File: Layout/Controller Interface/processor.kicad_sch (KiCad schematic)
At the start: 27 parts, among them J1 USB_C_Receptacle_USB2.0, SW3 SW_PAIR, SW4 SW_BOOT, U1 W25Q32JVSS, U2 RP2040, Y2 Crystal_GND24

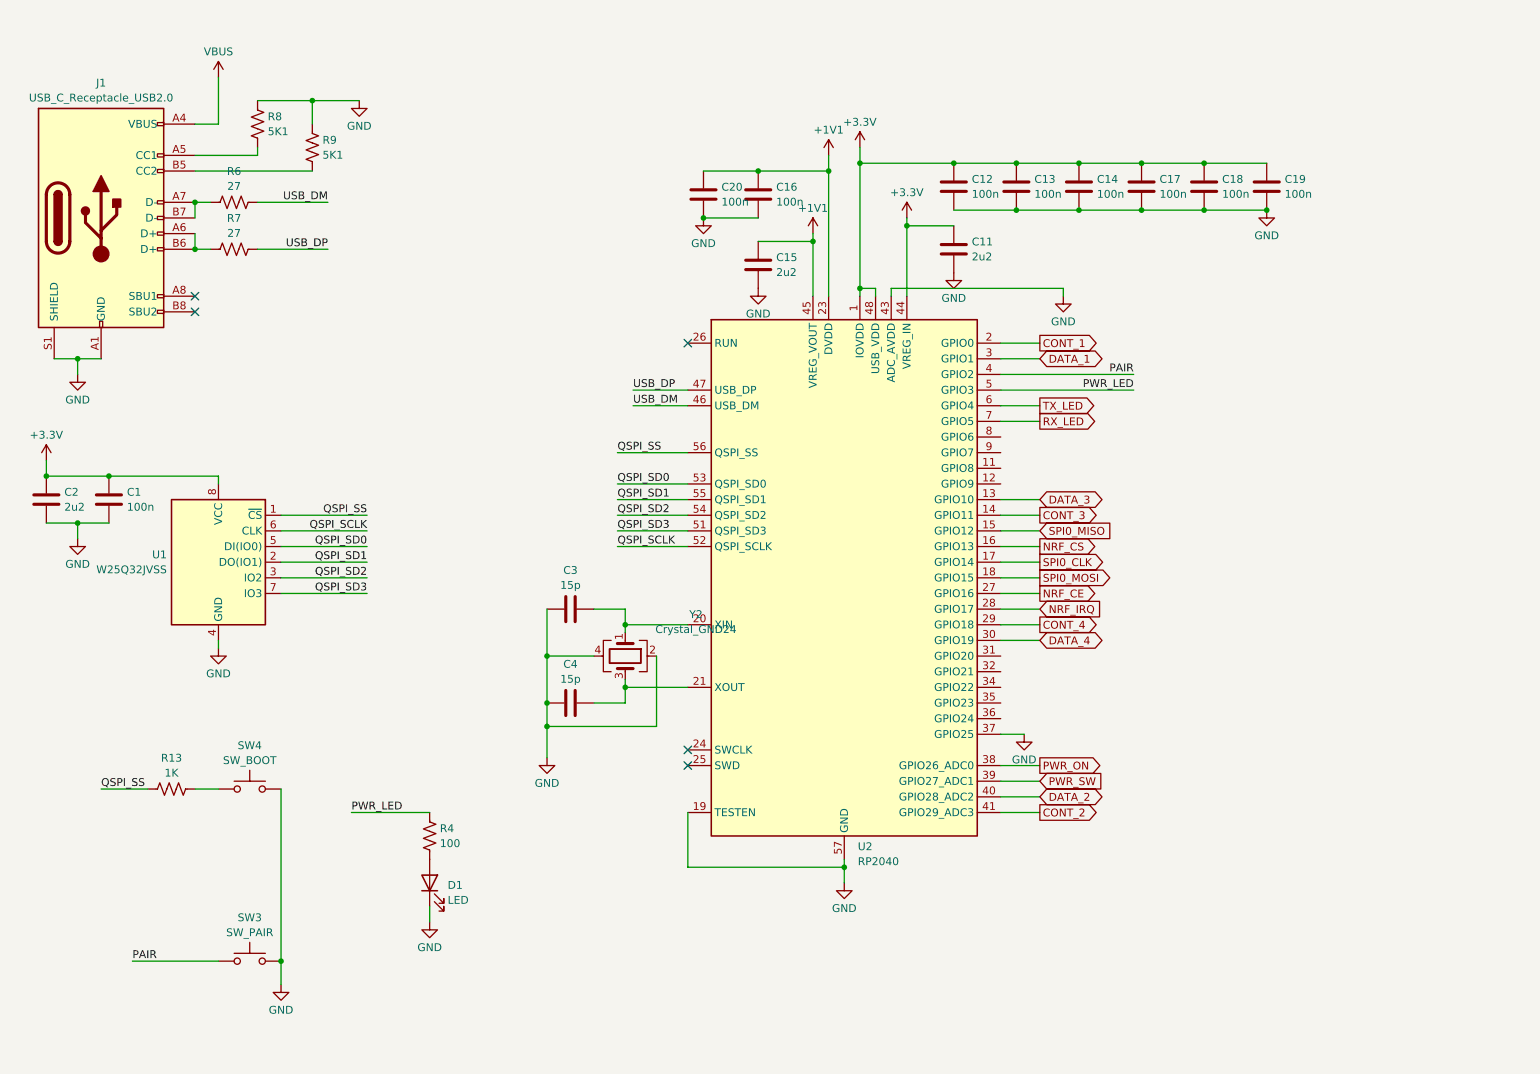
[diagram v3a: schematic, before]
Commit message: Create a separate board for the LEDs
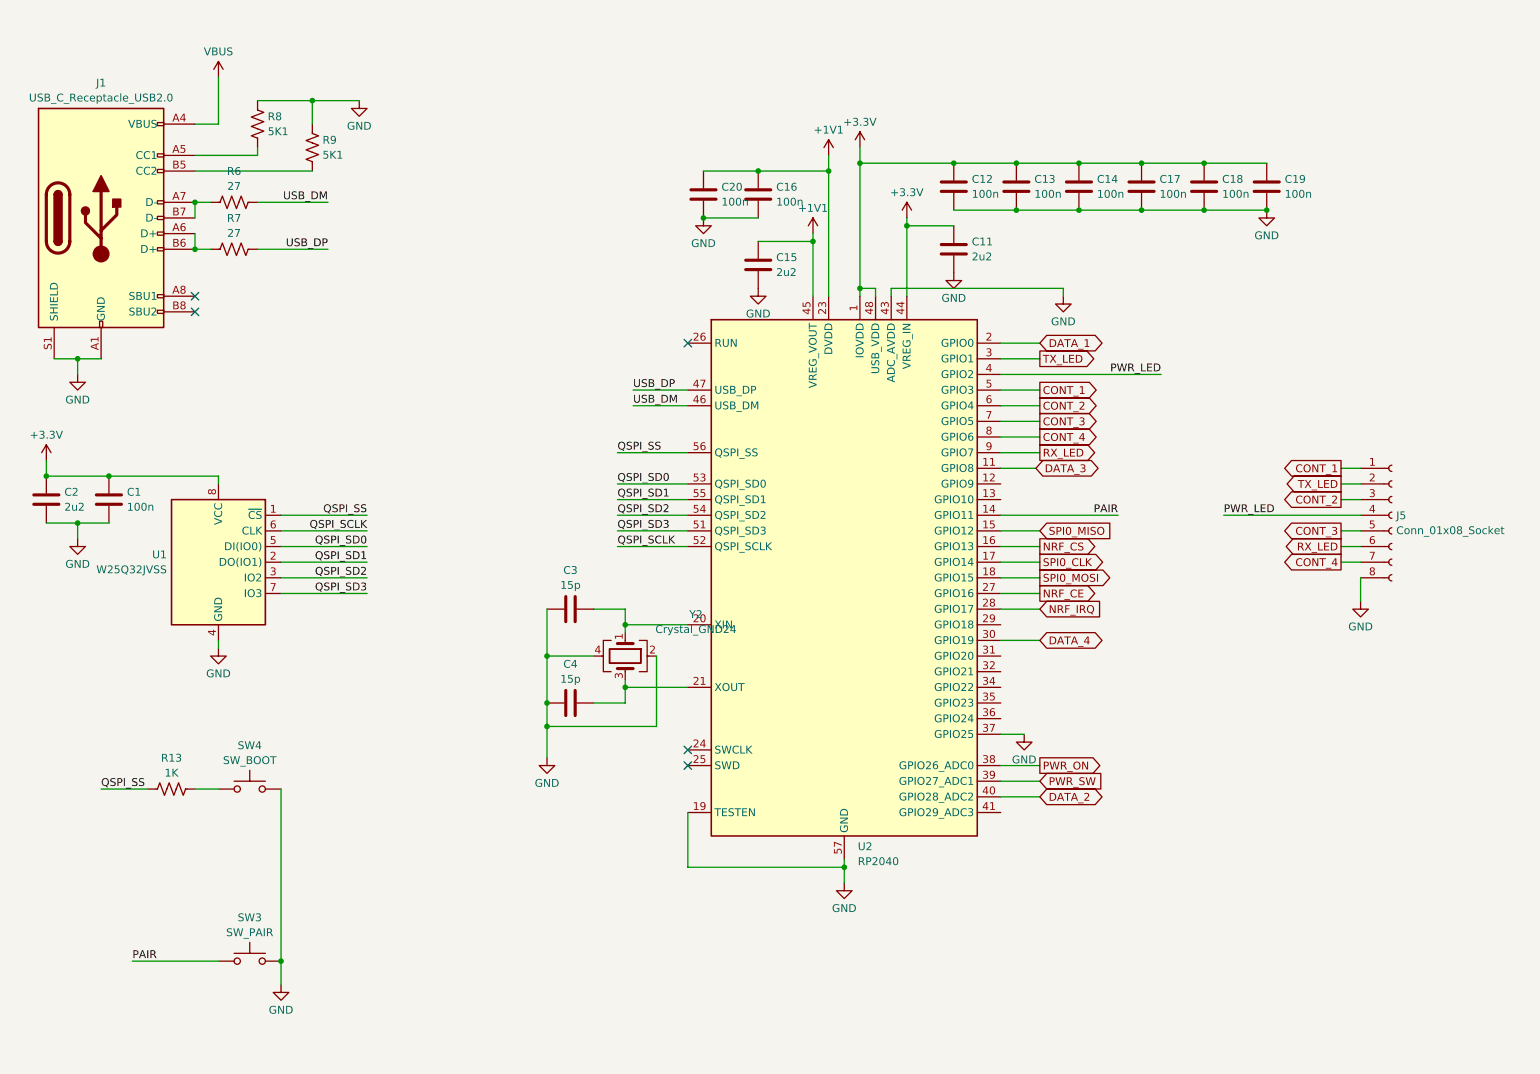
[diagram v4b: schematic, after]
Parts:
- removed D1: LED, LED_SMD:LED_0805_2012Metric, symbol Device:LED
- removed R4: 100, Resistor_SMD:R_0805_2012Metric, symbol Device:R_US
- added J5: Conn_01x08_Socket, Connector_PinSocket_1.00mm:PinSocket_2x04_P1.00mm_Vertical_SMD, symbol Connector:Conn_01x08_Socket
- SW3: footprint Button_Switch_SMD:SW_SPST_TL3342 -> Button_Switch_SMD:Panasonic_EVQPUK_EVQPUB
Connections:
- net CONT_1: now also U2.5 (GPIO3), J5.1 (Pin_1); no longer U2.2 (GPIO0)
- net CONT_2: now also U2.6 (GPIO4), J5.3 (Pin_3); no longer U2.41 (GPIO29_ADC3)
- net CONT_3: now also U2.7 (GPIO5), J5.5 (Pin_5); no longer U2.14 (GPIO11)
- net CONT_4: now also U2.8 (GPIO6), J5.7 (Pin_7); no longer U2.29 (GPIO18)
- net DATA_1: now also U2.2 (GPIO0); no longer U2.3 (GPIO1)
- net DATA_3: now also U2.11 (GPIO8); no longer U2.13 (GPIO10)
- net GND: now also J5.8 (Pin_8)
- net PAIR: now also U2.14 (GPIO11); no longer U2.4 (GPIO2)
- net PWR_LED: now also U2.4 (GPIO2), J5.4 (Pin_4); no longer U2.5 (GPIO3)
- net RX_LED: now also U2.9 (GPIO7), J5.6 (Pin_6); no longer U2.7 (GPIO5)
- net TX_LED: now also U2.3 (GPIO1), J5.2 (Pin_2); no longer U2.6 (GPIO4)
